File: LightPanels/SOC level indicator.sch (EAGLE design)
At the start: 156 parts

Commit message: No airwires
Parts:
- added C79, C84: 10uF, SparkFun-Capacitors:10UF-16V-10%(TANT)
- added IC1: LM1084-ADJ, lm1084-adj-to263:LM1084-ADJ
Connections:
- new net +12V: C84.+, IC1.IN
- net +5V: now also C79.+, IC1.OUT
- net GND: now also C79.-, C84.-

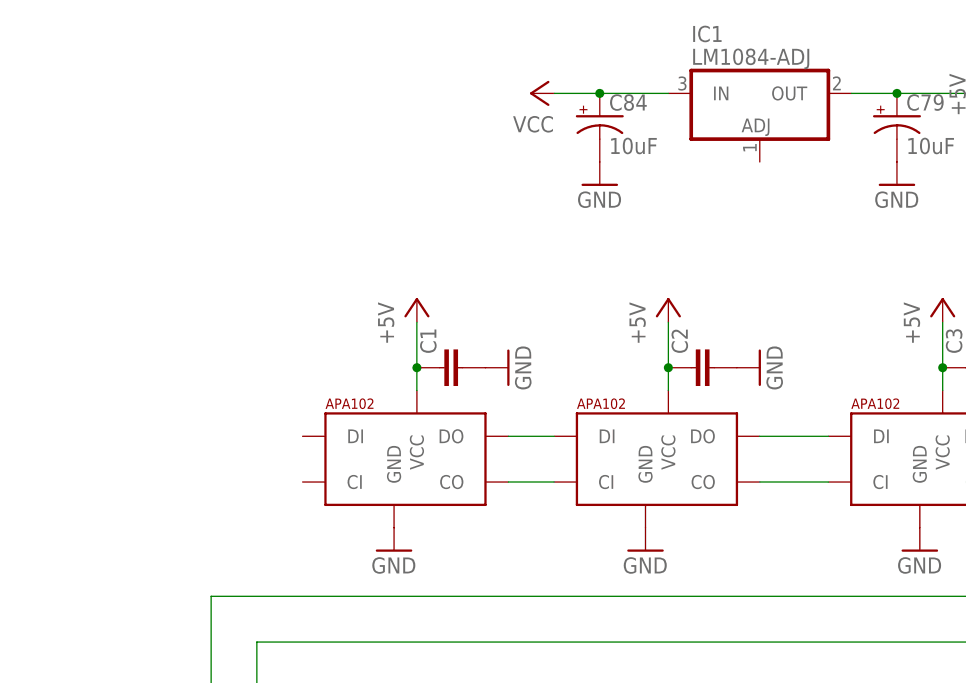
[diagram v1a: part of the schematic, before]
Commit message: SOC level indicator
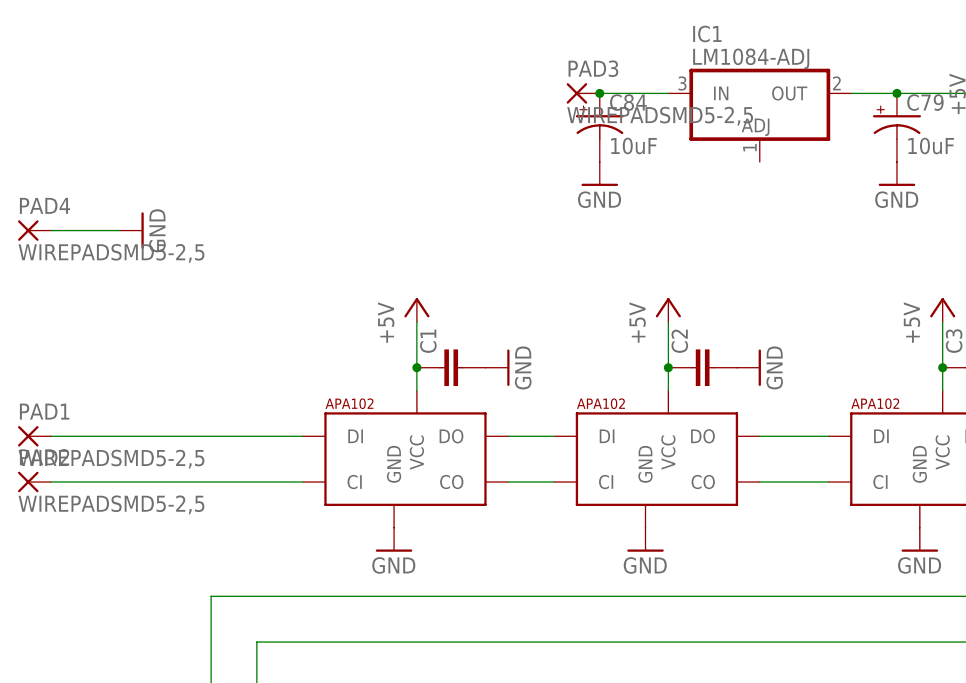
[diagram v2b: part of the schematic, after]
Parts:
- added PAD1, PAD2, PAD3, PAD4: WIREPADSMD5-2,5, wirepad:WIREPADSMD5-2,5
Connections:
- new net N$149: PAD1.P, U$1.DI
- new net N$150: PAD2.P, U$1.CI
- net +12V: now also PAD3.P
- net GND: now also PAD4.P
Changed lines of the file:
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@@
 <part name="C79" library="SparkFun-Capacitors" deviceset="10UF-16V-10%(TANT)" device="" value="10uF"/>
 <part name="GND158" library="supply1" deviceset="GND" device=""/>
-<part name="P+79" library="supply1" deviceset="VCC" device=""/>
 <part name="C84" library="SparkFun-Capacitors" deviceset="10UF-16V-10%(TANT)" device="" value="10uF"/>
 <part name="GND167" library="supply1" deviceset="GND" device=""/>
@@
 <part name="P+4" library="supply1" deviceset="+5V" device=""/>
 <part name="P+5" library="supply1" deviceset="+5V" device=""/>
+<part name="PAD1" library="wirepad" deviceset="WIREPAD" device="SMD5-2,5"/>
+<part name="PAD2" library="wirepad" deviceset="WIREPAD" device="SMD5-2,5"/>
+<part name="PAD3" library="wirepad" deviceset="WIREPAD" device="SMD5-2,5"/>
+<part name="PAD4" library="wirepad" deviceset="WIREPAD" device="SMD5-2,5"/>
+<part name="GND157" library="supply1" deviceset="GND" device=""/>
 </parts>
 <sheets>
@@
 <instance part="C79" gate="G$1" x="71.12" y="182.88"/>
 <instance part="GND158" gate="1" x="71.12" y="175.26"/>
-<instance part="P+79" gate="VCC" x="30.48" y="185.42" rot="R90"/>
 <instance part="C84" gate="G$1" x="38.1" y="182.88"/>
 <instance part="GND167" gate="1" x="38.1" y="175.26"/>
@@
 <instance part="P+4" gate="1" x="76.2" y="162.56"/>
 <instance part="P+5" gate="1" x="104.14" y="162.56"/>
+<instance part="PAD1" gate="G$1" x="-25.4" y="147.32"/>
+<instance part="PAD2" gate="G$1" x="-25.4" y="142.24"/>
+<instance part="PAD3" gate="G$1" x="35.56" y="185.42"/>
+<instance part="PAD4" gate="G$1" x="-25.4" y="170.18"/>
+<instance part="GND157" gate="1" x="-12.7" y="170.18" rot="R90"/>
 </instances>
 <busses>
@@
 <pinref part="C84" gate="G$1" pin="-"/>
 <pinref part="GND167" gate="1" pin="GND"/>
+</segment>
+<segment>
+<pinref part="GND157" gate="1" pin="GND"/>
+<pinref part="PAD4" gate="G$1" pin="P"/>
+<wire x1="-22.86" y1="170.18" x2="-15.24" y2="170.18" width="0.1524" layer="91"/>
 </segment>
 </net>
@@
 <net name="+12V" class="0">
 <segment>
-<pinref part="P+79" gate="VCC" pin="VCC"/>
-<wire x1="33.02" y1="185.42" x2="38.1" y2="185.42" width="0.1524" layer="91"/>
 <pinref part="C84" gate="G$1" pin="+"/>
 <wire x1="38.1" y1="185.42" x2="45.72" y2="185.42" width="0.1524" layer="91"/>
+<pinref part="IC1" gate="G$1" pin="IN"/>
+<pinref part="PAD3" gate="G$1" pin="P"/>
 <junction x="38.1" y="185.42"/>
-<pinref part="IC1" gate="G$1" pin="IN"/>
 </segment>
 </net>
@@
 </segment>
 </net>
+<net name="N$149" class="0">
+<segment>
+<pinref part="U$1" gate="G$1" pin="DI"/>
+<pinref part="PAD1" gate="G$1" pin="P"/>
+<wire x1="-22.86" y1="147.32" x2="5.08" y2="147.32" width="0.1524" layer="91"/>
+</segment>
+</net>
+<net name="N$150" class="0">
+<segment>
+<pinref part="U$1" gate="G$1" pin="CI"/>
+<pinref part="PAD2" gate="G$1" pin="P"/>
+<wire x1="-22.86" y1="142.24" x2="5.08" y2="142.24" width="0.1524" layer="91"/>
+</segment>
+</net>
